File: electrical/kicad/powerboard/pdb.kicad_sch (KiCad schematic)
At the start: 46 parts

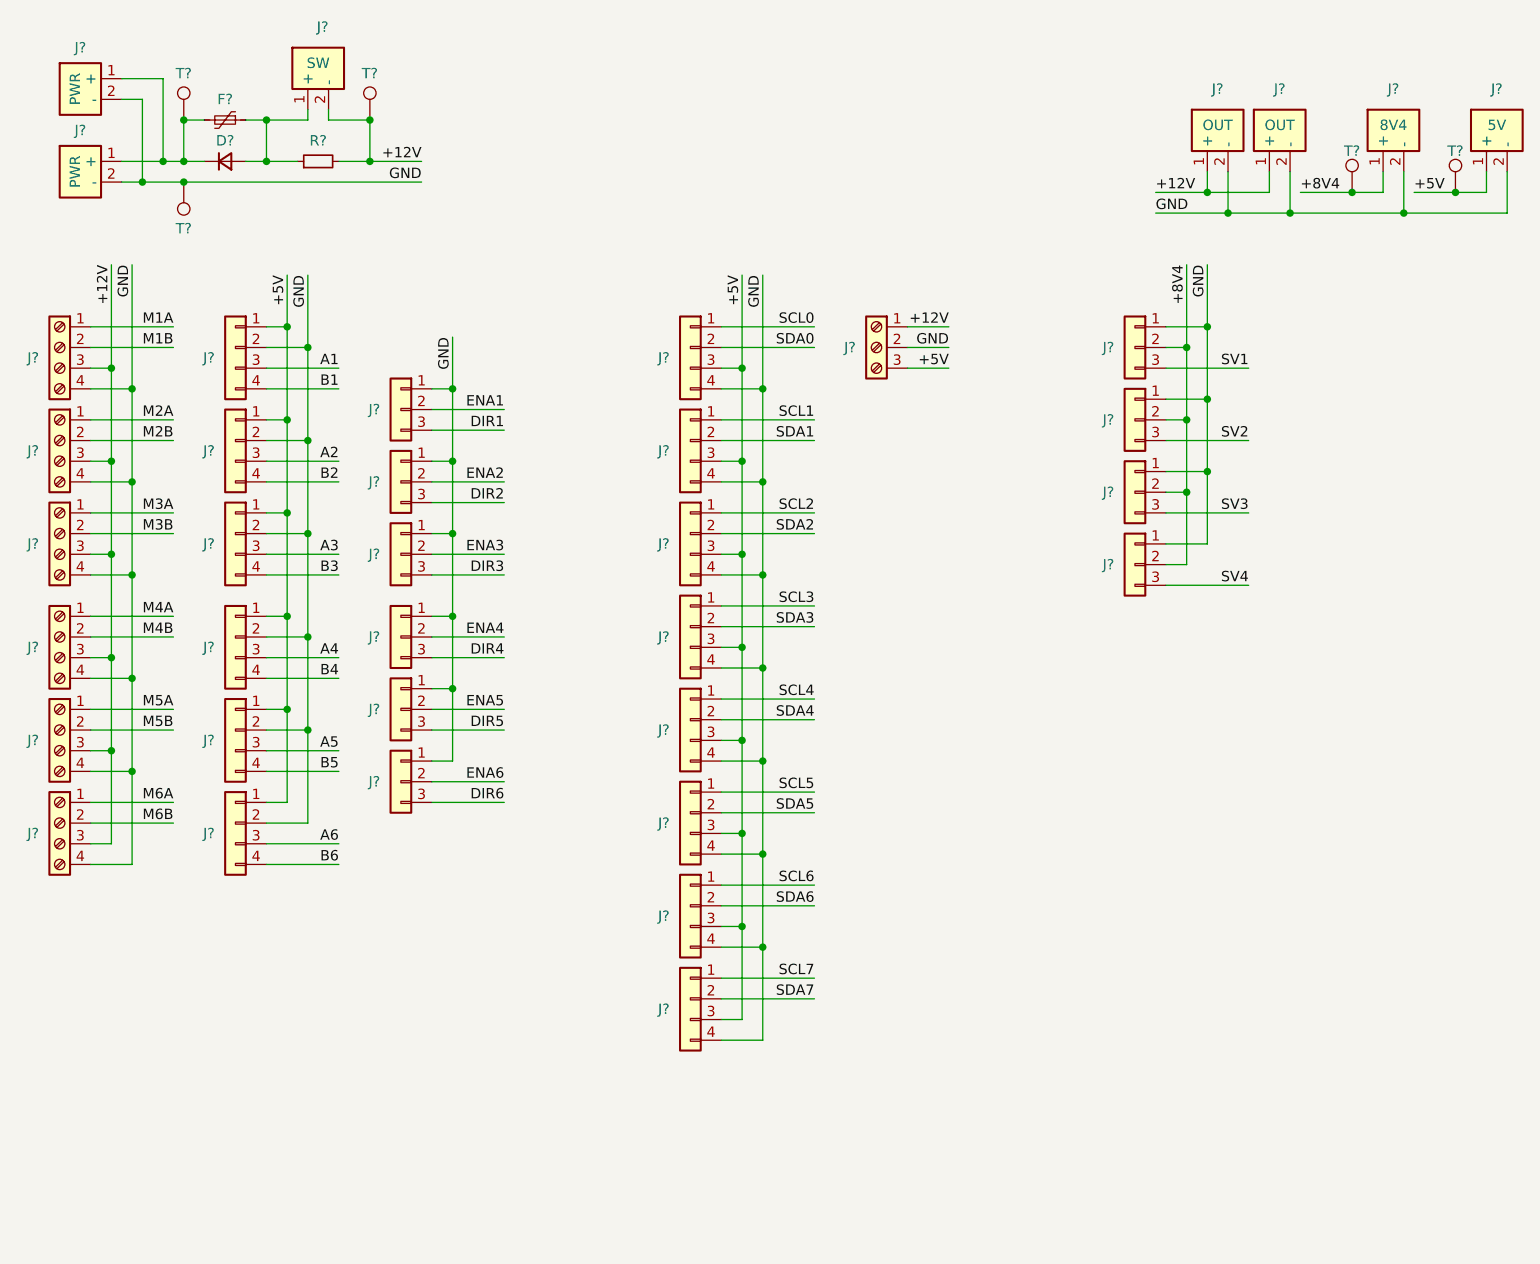
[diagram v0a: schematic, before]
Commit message: refactor: remove redundant submodules and update .gitignore
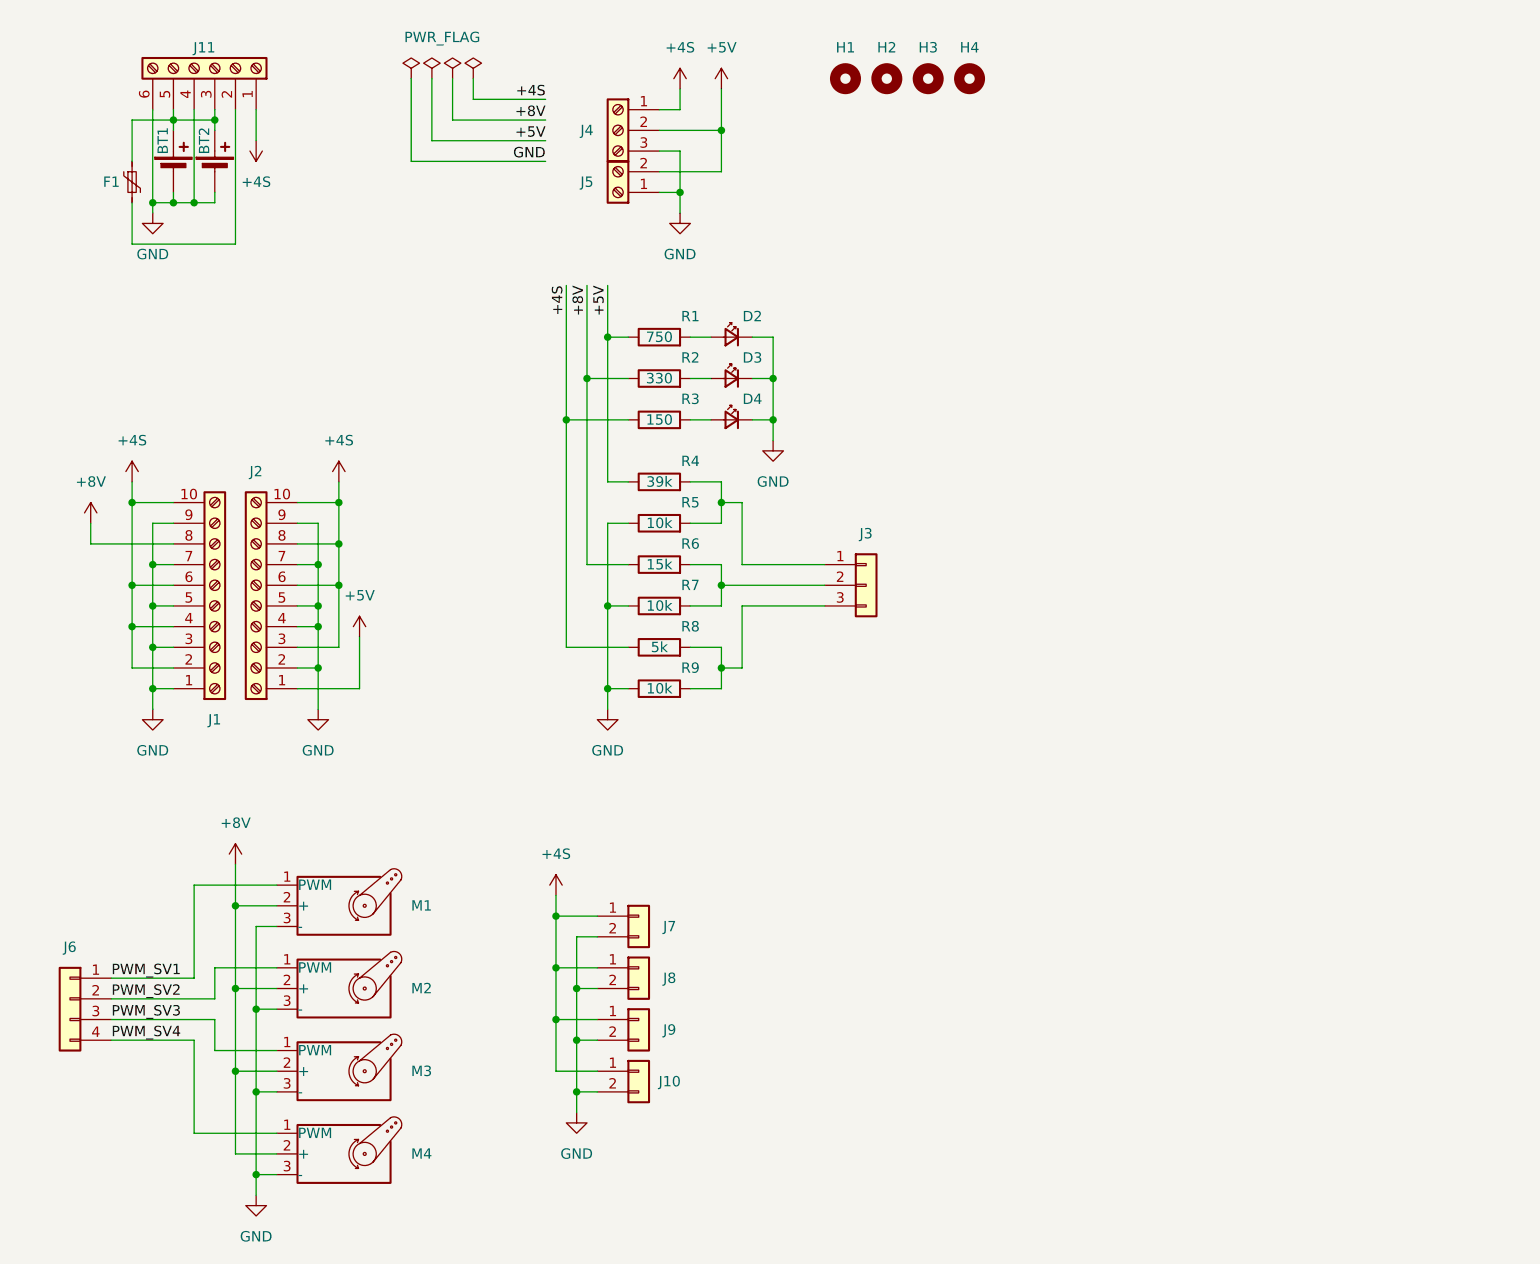
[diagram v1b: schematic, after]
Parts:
- removed D?: D_Small, symbol Device:D_Small
- removed F?: Polyfuse_Small, symbol Device:Polyfuse_Small
- removed J? (x14): Conn_01x04, symbol Connector_Generic:Conn_01x04
- removed J? (x6): Screw_Terminal_01x04, symbol Connector:Screw_Terminal_01x04
- removed J?: SW, XT60PW-M:AMASS_XT60PW-M, symbol Connectors:XT60PW-M
- removed J?: 5V, XT60PW-M:AMASS_XT60PW-M, symbol Connectors:XT60PW-M
- removed J? (x10): Conn_01x03, symbol Connector_Generic:Conn_01x03
- removed J? (x2): PWR, XT60PW-M:AMASS_XT60PW-M, symbol Connectors:XT60PW-M
- removed J? (x2): OUT, XT60PW-M:AMASS_XT60PW-M, symbol Connectors:XT60PW-M
- removed J?: Screw_Terminal_01x03, symbol Connector:Screw_Terminal_01x03
- removed J?: 8V4, XT60PW-M:AMASS_XT60PW-M, symbol Connectors:XT60PW-M
- removed R?: R_Small, symbol Device:R_Small
- removed T? (x5): TestPoint, symbol Connector:TestPoint
- added BT1, BT2: Battery_Cell, Connector_Phoenix_MSTB:PhoenixContact_MSTBA_2,5_2-G-5,08_1x02_P5.08mm_Horizontal, symbol Device:Battery_Cell
- added D2, D3, D4: LED_Small, LED_THT:LED_D3.0mm_Clear, symbol Device:LED_Small
- added F1: Polyfuse_Small, Fuses_THT:Fuse_Tyco_RGEF1400, symbol Device:Polyfuse_Small
- added H1, H2, H3, H4: MountingHole, MountingHole:MountingHole_3.2mm_M3, symbol Mechanical:MountingHole
- added J1, J2: Screw_Terminal_01x10, Connector_Phoenix_MSTB:PhoenixContact_MSTBA_2,5_10-G-5,08_1x10_P5.08mm_Horizontal, symbol Connector:Screw_Terminal_01x10
- added J10, J7, J8, J9: Conn_01x02, Connector_PinHeader_2.54mm:PinHeader_1x02_P2.54mm_Vertical, symbol Connector_Generic:Conn_01x02
- added J11: Screw_Terminal_01x06, Connector_Phoenix_MSTB:PhoenixContact_MSTBA_2,5_6-G-5,08_1x06_P5.08mm_Horizontal, symbol Connector:Screw_Terminal_01x06
- added J3: Conn_01x03, Connectors_JST:JST_XH_1x03_P2.54mm_Vertical, symbol Connector_Generic:Conn_01x03
- added J4: Screw_Terminal_01x03, Connector_Phoenix_MSTB:PhoenixContact_MSTBA_2,5_3-G-5,08_1x03_P5.08mm_Horizontal, symbol Connector:Screw_Terminal_01x03
- added J5: Screw_Terminal_01x02, Connector_Phoenix_MSTB:PhoenixContact_MSTBA_2,5_2-G-5,08_1x02_P5.08mm_Horizontal, symbol Connector:Screw_Terminal_01x02
- added J6: Conn_01x04, Connectors_JST:JST_XH_1x04_P2.54mm_Vertical, symbol Connector_Generic:Conn_01x04
- added M1, M2, M3, M4: Motor_Servo, Connector_PinHeader_2.54mm:PinHeader_1x03_P2.54mm_Vertical, symbol Motor:Motor_Servo
- added R1: 750, Resistor_THT:R_Axial_DIN0207_L6.3mm_D2.5mm_P7.62mm_Horizontal, symbol Device:R
- added R2: 330, Resistor_THT:R_Axial_DIN0207_L6.3mm_D2.5mm_P7.62mm_Horizontal, symbol Device:R
- added R3: 150, Resistor_THT:R_Axial_DIN0207_L6.3mm_D2.5mm_P7.62mm_Horizontal, symbol Device:R
- added R4: 39k, Resistor_THT:R_Axial_DIN0207_L6.3mm_D2.5mm_P7.62mm_Horizontal, symbol Device:R
- added R5, R7, R9: 10k, Resistor_THT:R_Axial_DIN0207_L6.3mm_D2.5mm_P7.62mm_Horizontal, symbol Device:R
- added R6: 15k, Resistor_THT:R_Axial_DIN0207_L6.3mm_D2.5mm_P7.62mm_Horizontal, symbol Device:R
- added R8: 5k, Resistor_THT:R_Axial_DIN0207_L6.3mm_D2.5mm_P7.62mm_Horizontal, symbol Device:R
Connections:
- net +5V: now also J2.1 (Pin_1), J4.2 (Pin_2), J5.2 (Pin_2), R1.1, R4.1
- net GND: now also BT1.2 (-), BT2.2 (-), D2.1 (K), D3.1 (K), D4.1 (K), J1.1 (Pin_1), J1.3 (Pin_3), J1.5 (Pin_5), J1.7 (Pin_7), J1.9 (Pin_9), J10.2 (Pin_2), J11.4 (Pin_4), J11.6 (Pin_6), J2.2 (Pin_2), J2.4 (Pin_4), J2.5 (Pin_5), J2.7 (Pin_7), J2.9 (Pin_9), J4.3 (Pin_3), J5.1 (Pin_1), J7.2 (Pin_2), J8.2 (Pin_2), J9.2 (Pin_2), M1.3 (-), M2.3 (-), M3.3 (-), M4.3 (-), R5.1, R7.1, R9.1
- new net: BT1.1 (+), BT2.1 (+), F1.1, J11.3 (Pin_3), J11.5 (Pin_5)
- new net: D3.2 (A), R2.2
- new net: J3.2 (Pin_2), R6.2, R7.2
- new net: J3.1 (Pin_1), R4.2, R5.2
- new net: J3.3 (Pin_3), R8.2, R9.2
- new net: D2.2 (A), R1.2
- new net: D4.2 (A), R3.2
- new net: F1.2, J11.2 (Pin_2)
- new net +4S: J1.10 (Pin_10), J1.2 (Pin_2), J1.4 (Pin_4), J1.6 (Pin_6), J10.1 (Pin_1), J11.1 (Pin_1), J2.10 (Pin_10), J2.3 (Pin_3), J2.6 (Pin_6), J2.8 (Pin_8), J4.1 (Pin_1), J7.1 (Pin_1), J8.1 (Pin_1), J9.1 (Pin_1), R3.1, R8.1
- new net +8V: J1.8 (Pin_8), M1.2 (+), M2.2 (+), M3.2 (+), M4.2 (+), R2.1, R6.1
- new net PWM_SV1: J6.1 (Pin_1), M1.1 (PWM)
- new net PWM_SV2: J6.2 (Pin_2), M2.1 (PWM)
- new net PWM_SV3: J6.3 (Pin_3), M3.1 (PWM)
- new net PWM_SV4: J6.4 (Pin_4), M4.1 (PWM)
